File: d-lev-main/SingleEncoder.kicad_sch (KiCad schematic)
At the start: 4 parts, among them SW1 RotaryEncoder_Switch

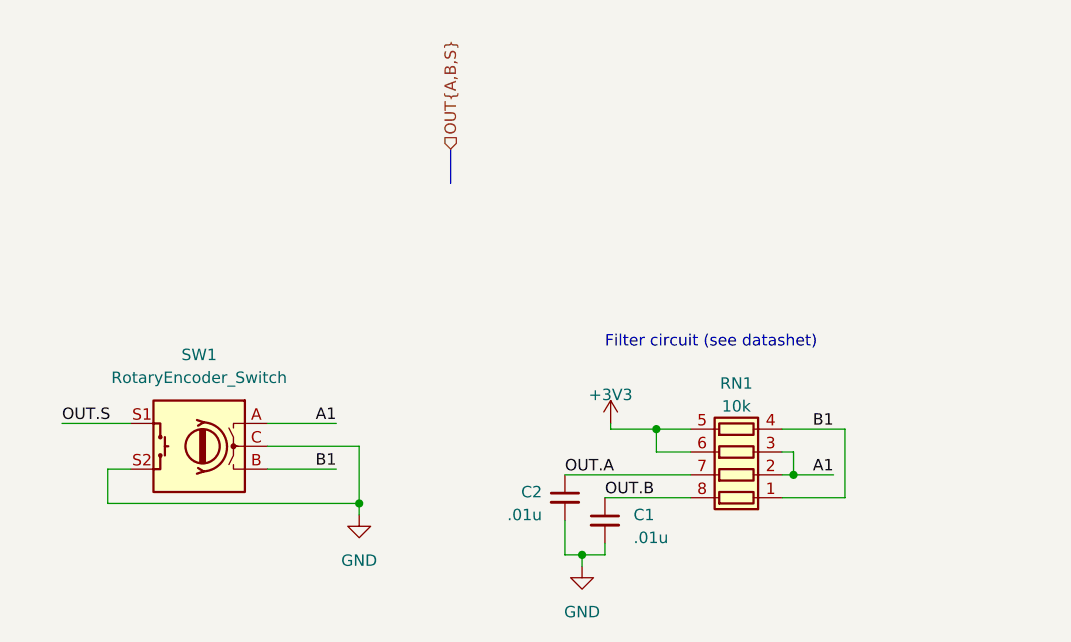
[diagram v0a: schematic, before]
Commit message: more encoder bus mangling
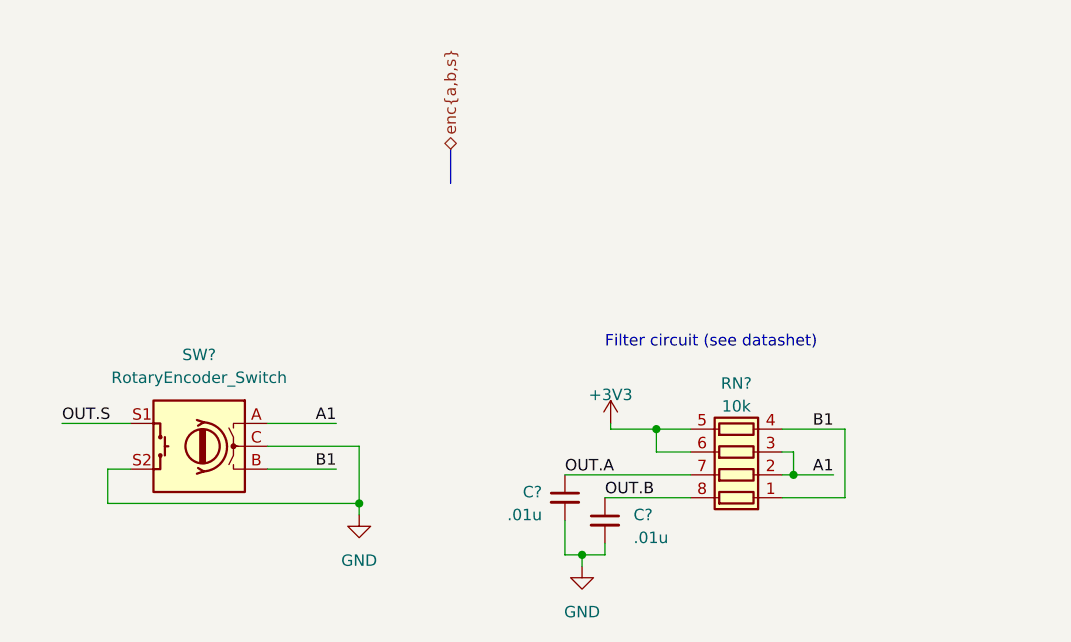
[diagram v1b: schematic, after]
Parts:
- renumbered C1 to C?, C2 to C?, RN1 to RN?, SW1 to SW?

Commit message: Small changes to 3D models and footprints; fixed bus routing of encoder signals
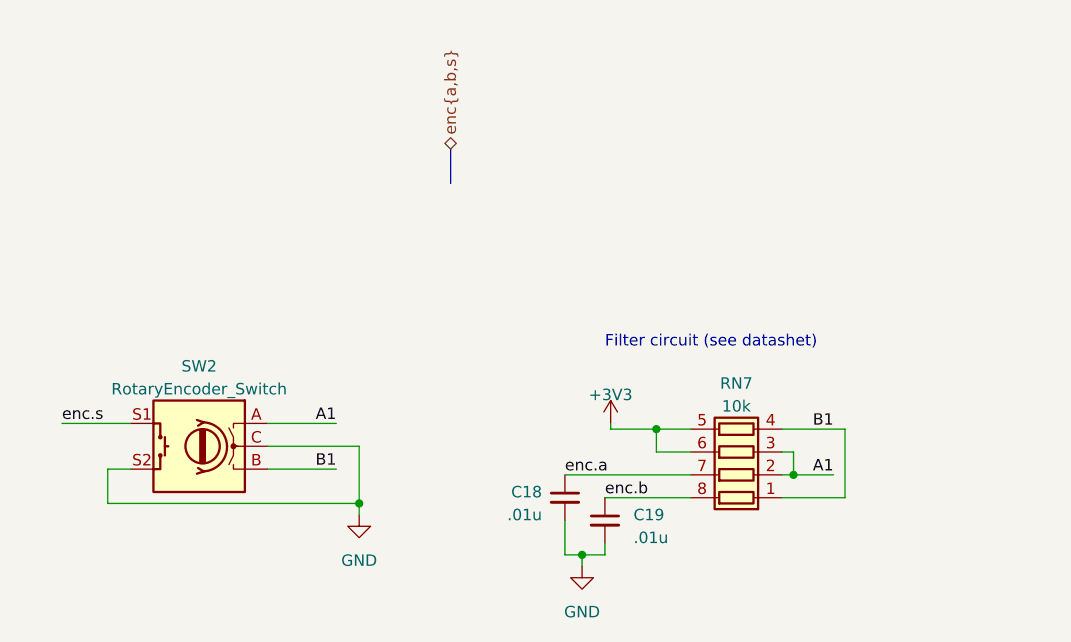
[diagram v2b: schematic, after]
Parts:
- SW2: renamed from SW?; footprint d-lev:PEC11S9215FS0015 -> d-lev:PEC11S-929K; symbol Device:RotaryEncoder_Switch -> assorted:RotaryEncoder_Switch_MountingPad
- gave numbers to parts that had none: 3
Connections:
- net OUT.A renamed enc.a
- net OUT.B renamed enc.b
- net OUT.S renamed enc.s

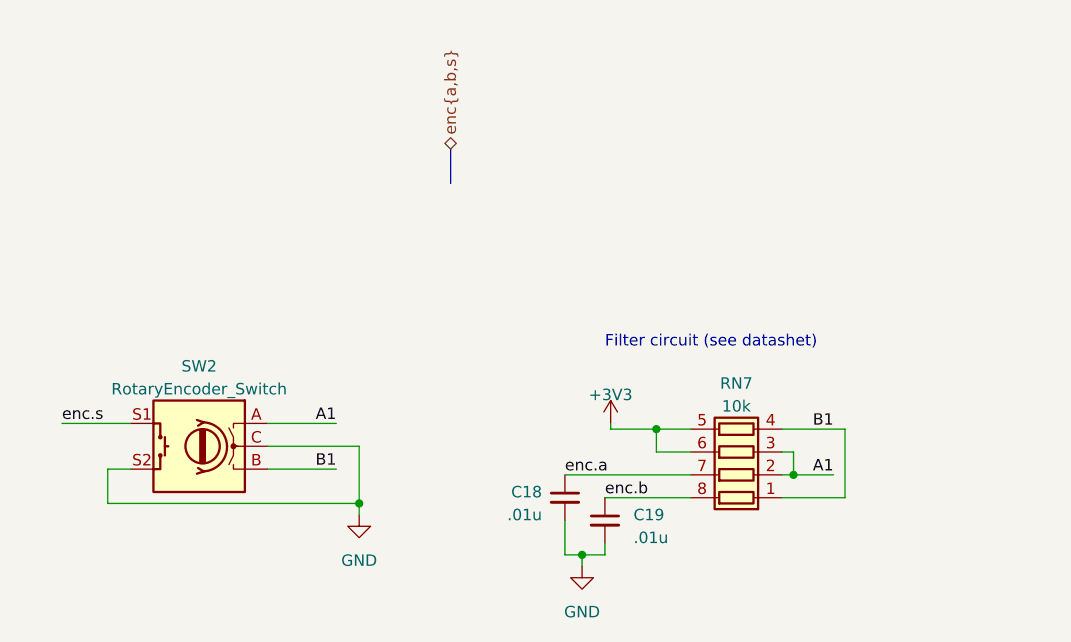
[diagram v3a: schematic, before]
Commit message: start routing
* add simple knob model
* place encoders
* change display to use SMT female headers and SMTSO screw holes
* rotate fpga model 90 degrees
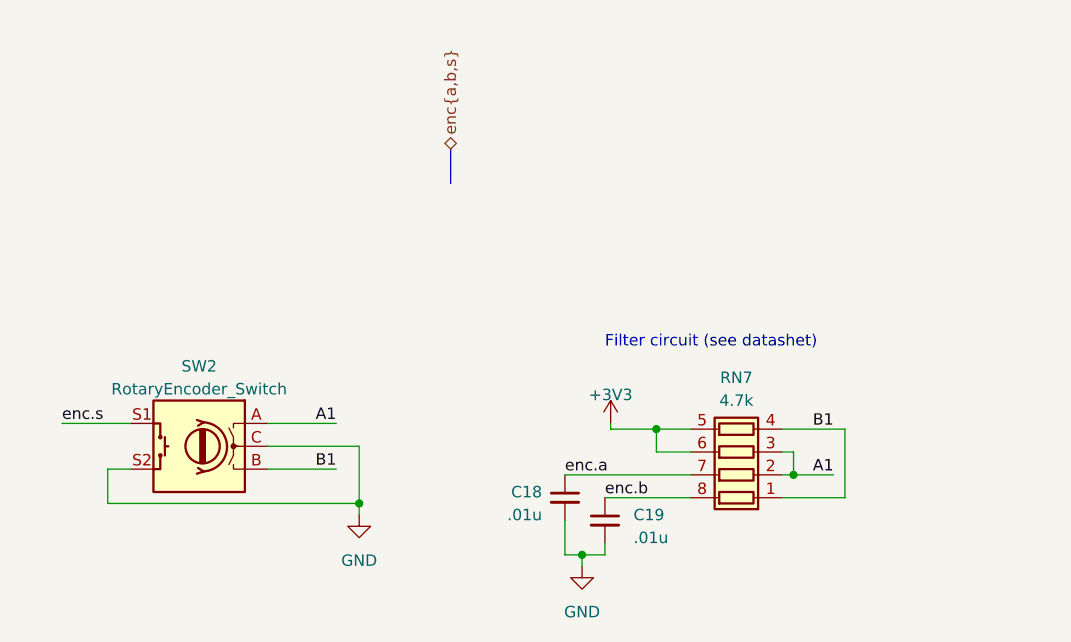
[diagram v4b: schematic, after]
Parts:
- C18, C19: footprint Capacitor_SMD:C_0805_2012Metric_Pad1.18x1.45mm_HandSolder -> Capacitor_SMD:C_0603_1608Metric
- RN7: value 10k -> 4.7k
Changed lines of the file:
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@@
       (effects (font (size 1.27 1.27)) (justify left))
     )
-    (property "Footprint" "Capacitor_SMD:C_0805_2012Metric_Pad1.18x1.45mm_HandSolder" (at 161.925 112.395 0)
+    (property "Footprint" "Capacitor_SMD:C_0603_1608Metric" (at 161.925 112.395 0)
       (effects (font (size 1.27 1.27)) hide)
     )
@@
       (effects (font (size 1.27 1.27)) (justify right))
     )
-    (property "Footprint" "Capacitor_SMD:C_0805_2012Metric_Pad1.18x1.45mm_HandSolder" (at 157.48 109.855 0)
+    (property "Footprint" "Capacitor_SMD:C_0603_1608Metric" (at 157.48 109.855 0)
       (effects (font (size 1.27 1.27)) hide)
     )
@@
   (symbol (lib_id "Device:R_Pack04") (at 176.53 104.775 90) (unit 1)
     (in_bom yes) (on_board yes) (dnp no) (fields_autoplaced)
-    (property "Reference" "RN7" (at 176.53 97.155 90)
+    (property "Reference" "RN7" (at 176.53 96.52 90)
       (effects (font (size 1.27 1.27)))
     )
-    (property "Value" "10k" (at 176.53 99.695 90)
+    (property "Value" "4.7k" (at 176.53 99.06 90)
       (effects (font (size 1.27 1.27)))
     )

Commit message: many changes to pcb
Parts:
- renumbered C18 to C3, C19 to C4, RN7 to RN2
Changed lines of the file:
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@@
   (symbol (lib_id "Device:C_Small") (at 161.925 112.395 0) (unit 1)
     (in_bom yes) (on_board yes) (dnp no) (fields_autoplaced)
-    (property "Reference" "C19" (at 165.1 111.7663 0)
+    (property "Reference" "C4" (at 165.1 111.7663 0)
       (effects (font (size 1.27 1.27)) (justify left))
     )
@@
       (project "dlev-mini"
         (path "/eb5e8bfd-9871-4528-bf57-58851bf63907/cff6c4c6-3203-4cdb-bbe2-98a8d2d1dddc"
-          (reference "C19") (unit 1)
+          (reference "C4") (unit 1)
         )
         (path "/eb5e8bfd-9871-4528-bf57-58851bf63907/0349b78d-0ccc-461e-9db6-1e1bc7d0ccab"
@@
         )
         (path "/eb5e8bfd-9871-4528-bf57-58851bf63907/9838bf98-d031-4cc3-a292-df93f66081f4"
-          (reference "C4") (unit 1)
-        )
-        (path "/eb5e8bfd-9871-4528-bf57-58851bf63907/ecc3d972-8081-426f-8ae3-c9695eae3f84"
           (reference "C6") (unit 1)
         )
-        (path "/eb5e8bfd-9871-4528-bf57-58851bf63907/15bc2a13-566b-404a-831d-584fbcfc8c8b"
-          (reference "C13") (unit 1)
-        )
-        (path "/eb5e8bfd-9871-4528-bf57-58851bf63907/010066a8-ac88-4d5d-a4fc-14579e6b5c08"
-          (reference "C17") (unit 1)
-        )
-        (path "/eb5e8bfd-9871-4528-bf57-58851bf63907/e62df110-b9e6-4d89-9c0c-e50e20fc8385"
-          (reference "C21") (unit 1)
-        )
-        (path "/eb5e8bfd-9871-4528-bf57-58851bf63907/896930f5-d9a7-4b6b-9e53-0b8ea5eb94db"
-          (reference "C15") (unit 1)
+        (path "/eb5e8bfd-9871-4528-bf57-58851bf63907/ecc3d972-8081-426f-8ae3-c9695eae3f84"
+          (reference "C8") (unit 1)
+        )
+        (path "/eb5e8bfd-9871-4528-bf57-58851bf63907/15bc2a13-566b-404a-831d-584fbcfc8c8b"
+          (reference "C10") (unit 1)
+        )
+        (path "/eb5e8bfd-9871-4528-bf57-58851bf63907/010066a8-ac88-4d5d-a4fc-14579e6b5c08"
+          (reference "C14") (unit 1)
+        )
+        (path "/eb5e8bfd-9871-4528-bf57-58851bf63907/e62df110-b9e6-4d89-9c0c-e50e20fc8385"
+          (reference "C16") (unit 1)
+        )
+        (path "/eb5e8bfd-9871-4528-bf57-58851bf63907/896930f5-d9a7-4b6b-9e53-0b8ea5eb94db"
+          (reference "C12") (unit 1)
         )
       )
@@
   (symbol (lib_id "Device:C_Small") (at 157.48 109.855 0) (unit 1)
     (in_bom yes) (on_board yes) (dnp no) (fields_autoplaced)
-    (property "Reference" "C18" (at 154.94 109.2263 0)
+    (property "Reference" "C3" (at 154.94 109.2263 0)
       (effects (font (size 1.27 1.27)) (justify right))
     )
@@
       (project "dlev-mini"
         (path "/eb5e8bfd-9871-4528-bf57-58851bf63907/cff6c4c6-3203-4cdb-bbe2-98a8d2d1dddc"
-          (reference "C18") (unit 1)
+          (reference "C3") (unit 1)
         )
         (path "/eb5e8bfd-9871-4528-bf57-58851bf63907/0349b78d-0ccc-461e-9db6-1e1bc7d0ccab"
@@
         )
         (path "/eb5e8bfd-9871-4528-bf57-58851bf63907/9838bf98-d031-4cc3-a292-df93f66081f4"
-          (reference "C3") (unit 1)
-        )
-        (path "/eb5e8bfd-9871-4528-bf57-58851bf63907/ecc3d972-8081-426f-8ae3-c9695eae3f84"
           (reference "C5") (unit 1)
         )
-        (path "/eb5e8bfd-9871-4528-bf57-58851bf63907/15bc2a13-566b-404a-831d-584fbcfc8c8b"
-          (reference "C12") (unit 1)
-        )
-        (path "/eb5e8bfd-9871-4528-bf57-58851bf63907/010066a8-ac88-4d5d-a4fc-14579e6b5c08"
-          (reference "C16") (unit 1)
-        )
-        (path "/eb5e8bfd-9871-4528-bf57-58851bf63907/e62df110-b9e6-4d89-9c0c-e50e20fc8385"
-          (reference "C20") (unit 1)
-        )
-        (path "/eb5e8bfd-9871-4528-bf57-58851bf63907/896930f5-d9a7-4b6b-9e53-0b8ea5eb94db"
-          (reference "C14") (unit 1)
+        (path "/eb5e8bfd-9871-4528-bf57-58851bf63907/ecc3d972-8081-426f-8ae3-c9695eae3f84"
+          (reference "C7") (unit 1)
+        )
+        (path "/eb5e8bfd-9871-4528-bf57-58851bf63907/15bc2a13-566b-404a-831d-584fbcfc8c8b"
+          (reference "C9") (unit 1)
+        )
+        (path "/eb5e8bfd-9871-4528-bf57-58851bf63907/010066a8-ac88-4d5d-a4fc-14579e6b5c08"
+          (reference "C13") (unit 1)
+        )
+        (path "/eb5e8bfd-9871-4528-bf57-58851bf63907/e62df110-b9e6-4d89-9c0c-e50e20fc8385"
+          (reference "C15") (unit 1)
+        )
+        (path "/eb5e8bfd-9871-4528-bf57-58851bf63907/896930f5-d9a7-4b6b-9e53-0b8ea5eb94db"
+          (reference "C11") (unit 1)
         )
       )
@@
   (symbol (lib_id "Device:R_Pack04") (at 176.53 104.775 90) (unit 1)
     (in_bom yes) (on_board yes) (dnp no) (fields_autoplaced)
-    (property "Reference" "RN7" (at 176.53 96.52 90)
+    (property "Reference" "RN2" (at 176.53 96.52 90)
       (effects (font (size 1.27 1.27)))
     )
@@
       (project "dlev-mini"
         (path "/eb5e8bfd-9871-4528-bf57-58851bf63907/cff6c4c6-3203-4cdb-bbe2-98a8d2d1dddc"
+          (reference "RN2") (unit 1)
+        )
+        (path "/eb5e8bfd-9871-4528-bf57-58851bf63907/0349b78d-0ccc-461e-9db6-1e1bc7d0ccab"
+          (reference "RN1") (unit 1)
+        )
+        (path "/eb5e8bfd-9871-4528-bf57-58851bf63907/9838bf98-d031-4cc3-a292-df93f66081f4"
+          (reference "RN3") (unit 1)
+        )
+        (path "/eb5e8bfd-9871-4528-bf57-58851bf63907/ecc3d972-8081-426f-8ae3-c9695eae3f84"
+          (reference "RN4") (unit 1)
+        )
+        (path "/eb5e8bfd-9871-4528-bf57-58851bf63907/15bc2a13-566b-404a-831d-584fbcfc8c8b"
+          (reference "RN5") (unit 1)
+        )
+        (path "/eb5e8bfd-9871-4528-bf57-58851bf63907/010066a8-ac88-4d5d-a4fc-14579e6b5c08"
           (reference "RN7") (unit 1)
         )
-        (path "/eb5e8bfd-9871-4528-bf57-58851bf63907/0349b78d-0ccc-461e-9db6-1e1bc7d0ccab"
-          (reference "RN1") (unit 1)
-        )
-        (path "/eb5e8bfd-9871-4528-bf57-58851bf63907/9838bf98-d031-4cc3-a292-df93f66081f4"
-          (reference "RN2") (unit 1)
-        )
-        (path "/eb5e8bfd-9871-4528-bf57-58851bf63907/ecc3d972-8081-426f-8ae3-c9695eae3f84"
-          (reference "RN3") (unit 1)
-        )
-        (path "/eb5e8bfd-9871-4528-bf57-58851bf63907/15bc2a13-566b-404a-831d-584fbcfc8c8b"
-          (reference "RN4") (unit 1)
-        )
-        (path "/eb5e8bfd-9871-4528-bf57-58851bf63907/010066a8-ac88-4d5d-a4fc-14579e6b5c08"
+        (path "/eb5e8bfd-9871-4528-bf57-58851bf63907/e62df110-b9e6-4d89-9c0c-e50e20fc8385"
+          (reference "RN8") (unit 1)
+        )
+        (path "/eb5e8bfd-9871-4528-bf57-58851bf63907/896930f5-d9a7-4b6b-9e53-0b8ea5eb94db"
           (reference "RN6") (unit 1)
         )
-        (path "/eb5e8bfd-9871-4528-bf57-58851bf63907/e62df110-b9e6-4d89-9c0c-e50e20fc8385"
-          (reference "RN8") (unit 1)
-        )
-        (path "/eb5e8bfd-9871-4528-bf57-58851bf63907/896930f5-d9a7-4b6b-9e53-0b8ea5eb94db"
-          (reference "RN5") (unit 1)
-        )
-      )
+      )

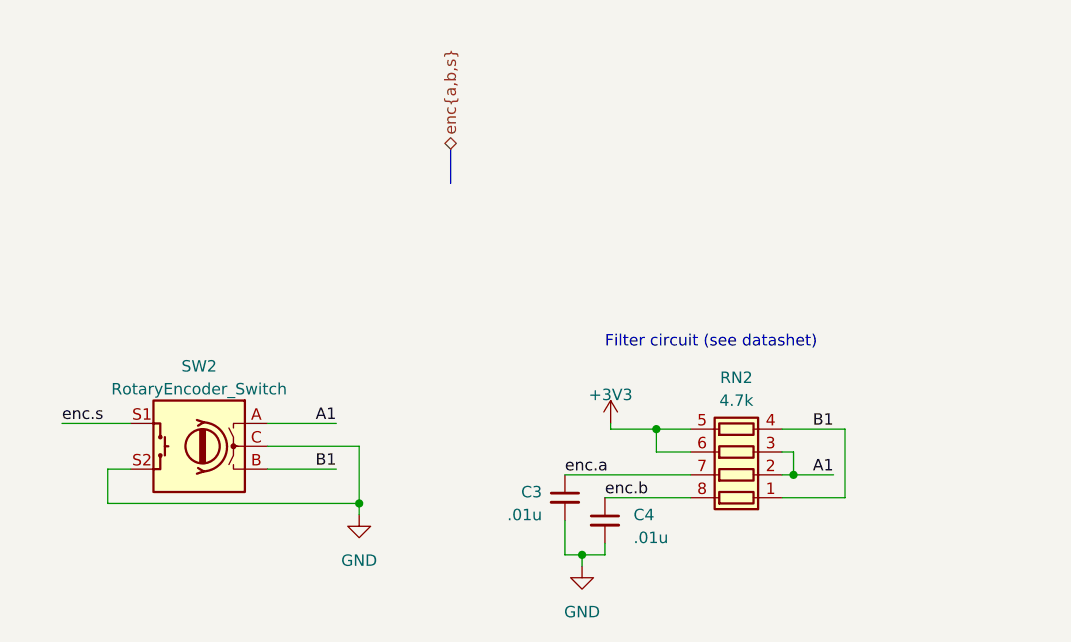
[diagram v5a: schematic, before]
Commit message: Switch from Rpacks to 0603 pull resistors
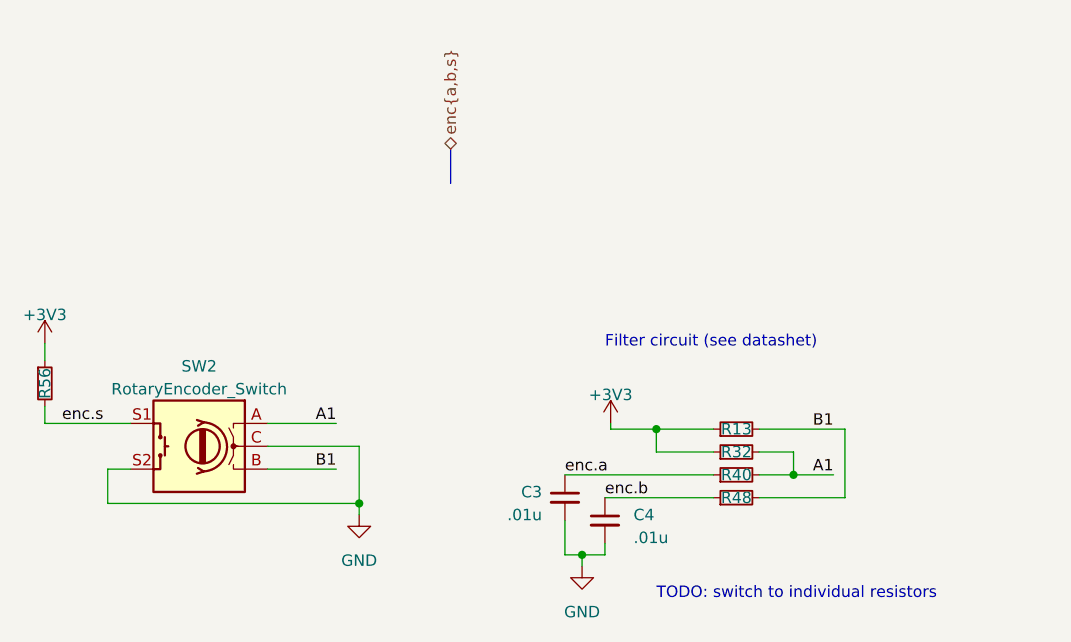
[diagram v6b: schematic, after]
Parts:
- removed RN2: 4.7k, Resistor_SMD:R_Array_Concave_4x0603, symbol Device:R_Pack04
- added R13, R32, R40, R48, R56: R_Small, Resistor_SMD:R_0603_1608Metric, symbol Device:R_Small
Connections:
- net +3V3: now also R13.1, R32.1, R56.1
- net A1: now also R32.2, R40.2
- net B1: now also R13.2, R48.2
- net enc.a: now also R40.1
- net enc.b: now also R48.1
- net enc.s: now also R56.2
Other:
- note added: "TODO: switch to individual resistors"

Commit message: Pinned out FPGA and rearranged encoders again
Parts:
- R13, R32, R40, R48, R56: value R_Small -> 10k
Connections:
- net A1: now also R13.2, R48.2; no longer R32.2, R40.2
- net B1: now also R32.2, R40.2; no longer R13.2, R48.2
- net enc.a: now also C4.1, R48.1; no longer C3.1, R40.1
- net enc.b: now also C3.1, R40.1; no longer C4.1, R48.1
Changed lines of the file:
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@@
     (effects (font (size 1.27 1.27)) (justify left bottom))
   )
-  (label "B1" (at 187.325 102.235 180) (fields_autoplaced)
+  (label "B1" (at 187.325 107.315 180) (fields_autoplaced)
     (effects (font (size 1.27 1.27)) (justify right bottom))
   )
-  (label "A1" (at 187.325 107.315 180) (fields_autoplaced)
+  (label "A1" (at 187.325 102.235 180) (fields_autoplaced)
     (effects (font (size 1.27 1.27)) (justify right bottom))
   )
@@
     (effects (font (size 1.27 1.27)) (justify left bottom))
   )
-  (label "enc.b" (at 161.925 109.855 0) (fields_autoplaced)
+  (label "enc.a" (at 161.925 109.855 0) (fields_autoplaced)
     (effects (font (size 1.27 1.27)) (justify left bottom))
   )
-  (label "enc.a" (at 157.48 107.315 0) (fields_autoplaced)
+  (label "enc.b" (at 157.48 107.315 0) (fields_autoplaced)
     (effects (font (size 1.27 1.27)) (justify left bottom))
   )
@@
       (effects (font (size 1.27 1.27)))
     )
-    (property "Value" "R_Small" (at 176.53 100.33 90)
+    (property "Value" "10k" (at 176.53 100.33 90)
       (effects (font (size 1.27 1.27)) hide)
     )
@@
       (effects (font (size 1.27 1.27)))
     )
-    (property "Value" "R_Small" (at 176.53 102.87 90)
+    (property "Value" "10k" (at 176.53 102.87 90)
       (effects (font (size 1.27 1.27)) hide)
     )
@@
       (effects (font (size 1.27 1.27)))
     )
-    (property "Value" "R_Small" (at 101.6 97.155 90)
+    (property "Value" "10k" (at 101.6 97.155 90)
       (effects (font (size 1.27 1.27)) hide)
     )
@@
       (effects (font (size 1.27 1.27)))
     )
-    (property "Value" "R_Small" (at 176.53 107.95 90)
+    (property "Value" "10k" (at 176.53 107.95 90)
       (effects (font (size 1.27 1.27)) hide)
     )
@@
       (effects (font (size 1.27 1.27)))
     )
-    (property "Value" "R_Small" (at 176.53 105.41 90)
-      (effects (font (size 1.27 1.27)) hide)
-    )
+    (property "Value" "10k" (at 176.53 105.41 90)
+      (effects (font (size 1.27 1.27)) hide)
+    )
